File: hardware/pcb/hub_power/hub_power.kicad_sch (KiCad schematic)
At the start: 54 parts, among them J1 XIAO, J10 BAT (JST-PH), J11 → 電源板, J12 → ハブ板, J13 USB-C, J2 OLED, J3 AS5600, J4 SPK IN, J5 SPK OUT, J6 REED, J7 TOGGLE, J8 BTN2, K31 G6S-2F DC5, Q1 MMUN2133LT1G, Q31 SS8050, U1 TPS61090RSAR, U2 MCP73871-2CCI/ML, U3 INA226AIDGSR

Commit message: Extended を 12 → 9 種類に減らす（$36.84 → $27.63）
🔒 2026-09-12 ユーザー「b でいいでしょ」。PowerBoost から写した定数のうち 3 つを Basic の値へ寄せた。
回路の意味はほとんど変えていない。

- R2 340kΩ（C17636・Extended）→ 330kΩ 0603 C23137（Basic）。
  LBO の閾値 0.5×(1+R1/R2) が 3.25V → 3.33V。80mV 早く知らせる側へ動く。
- R6 270kΩ（C17589・Extended）→ 220kΩ 0603 C22961、R7 100kΩ → 82kΩ 0603 C23254（どちらも Basic）。
  VPCC の分圧比 100/370=0.2703 → 82/302=0.2715 で差は 0.45%。
- C6 100µF 10V 1210（C23742・Extended・$0.45）→ 47µF 10V 1206 C96123（Basic・$0.27）を 2 個。
  Basic の 100µF は 6.3V 品しかなく、5.2V が掛かる所で耐圧を下げると残る容量が確実に減る
  （どれだけ減るかは曲線を見ていないので分からない）。耐圧 10V を保つため 2 個に分けた。
  ⚠ 足した C9 は PowerBoost に無い部品で、私が足したもの。

部品は表面実装 44 個・28 種類（Basic 19・Extended 9）。費用は約 $97 → 約 $88。

検査: check_sch 0 件・未配線 0・KiCad DRC のエラー 0（警告 99）・
      check_pcb は下限 0.15mm を割る組 0（いちばん近いのは 0.151mm）。
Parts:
- removed C31: 0.1uF, Capacitor_SMD:C_0805_2012Metric, symbol Device:C_Small
- removed D31: 1N4148W, Diode_SMD:D_SOD-123, symbol Diode:1N4148W
- removed J6: REED, Connector_PinHeader_2.54mm:PinHeader_1x02_P2.54mm_Vertical, symbol Connector_Generic:Conn_01x02
- removed R20: 1K, Resistor_SMD:R_0805_2012Metric, symbol Device:R_Small
- removed R41: 10m, Resistor_SMD:R_1206_3216Metric, symbol Device:R_Small
- removed R44: 5.1k, Resistor_SMD:R_0805_2012Metric, symbol Device:R_Small
- added J1: XIAO, Connector_PinHeader_2.54mm:PinHeader_1x07_P2.54mm_Vertical, symbol Connector_Generic:Conn_01x07
- added J11: → 電源板, Connector_PinHeader_2.54mm:PinHeader_1x07_P2.54mm_Vertical, symbol Connector_Generic:Conn_01x07
- added J13: USB-C, katanori:USB_C_HRO_TYPE-C-31-M-12_NoFrontLegs, symbol Connector:USB_C_Receptacle_USB2.0_16P
- added K31: G6S-2F DC5, Relay_SMD:Relay_DPDT_Omron_G6S-2F, symbol Relay:G6S-2
- added Q1: MMUN2133LT1G, Package_TO_SOT_SMD:SOT-23, symbol Transistor_BJT:Q_PNP_BRT_BEC
- added Q31: SS8050, Package_TO_SOT_SMD:SOT-23, symbol Transistor_BJT:MMBT3904
- added U3: INA226AIDGSR, Package_SO:TSSOP-10_3x3mm_P0.5mm, symbol Sensor_Energy:INA226
- C31: renamed from C32; Note relay_board C2・リードの跳ね止め -> relay_board C1
- C32: renamed from J4; value SPK IN -> 0.1uF; footprint Connector_JST:JST_PH_B2B-PH-K_1x02_P2.00mm_Vertical -> Capacitor_SMD:C_0805_2012Metric; symbol Connector_Generic:Conn_01x02 -> Device:C_Small; LCSC (none) -> C49678; Note IN（ReSpeakerから） -> relay_board C2・リードの跳ね止め
- C41: renamed from R42; value 10K -> 0.1uF; footprint Resistor_SMD:R_0805_2012Metric -> Capacitor_SMD:C_0805_2012Metric; symbol Device:R_Small -> Device:C_Small; LCSC C17414 -> C49678; Note I2C の引き上げ -> (none)
- C6: value 100uF -> 47uF; footprint Capacitor_SMD:C_1210_3225Metric -> Capacitor_SMD:C_1206_3216Metric; LCSC C23742 -> C96123; Note (none) -> PowerBoost C6（100µF 1210）の片割れ
- C7: renamed from R6; value 270K -> 10uF; footprint Resistor_SMD:R_0805_2012Metric -> Capacitor_SMD:C_0805_2012Metric; symbol Device:R_Small -> Device:C_Small; LCSC C17589 -> C15850
- C9: renamed from R3; value 1.87M -> 47uF; footprint Resistor_SMD:R_0805_2012Metric -> Capacitor_SMD:C_1206_3216Metric; symbol Device:R_Small -> Device:C_Small; LCSC C482988 -> C96123; Note (none) -> PowerBoost C6 の片割れ・私が足した（2026-09-12）
- D31: renamed from K31; value G6S-2F DC5 -> 1N4148W; footprint Relay_SMD:Relay_DPDT_Omron_G6S-2F -> Diode_SMD:D_SOD-123; symbol Relay:G6S-2 -> Diode:1N4148W; LCSC C16707 -> C81598; Note COM–NO を使う・NC は空き。2 回路のうち使うのは 1 回路だけ（もう 1 回路は未接続） -> relay_board D1・カソードが +5V（表面実装の 1N4148W）
- J10: renamed from J13; value USB-C -> BAT (JST-PH); footprint katanori:USB_C_HRO_TYPE-C-31-M-12_NoFrontLegs -> Connector_JST:JST_PH_S2B-PH-K_1x02_P2.00mm_Horizontal; symbol Connector:USB_C_Receptacle_USB2.0_16P -> Connector_Generic:Conn_01x02; LCSC C165948 -> (none); Note 充電の口。D+/D− と SBU は使わない -> 🔴 1 番が −・2 番が +（PowerBoost B1 の並び）
- J4: renamed from J5; value SPK OUT -> SPK IN; Note OUT（スピーカーへ） -> IN（ReSpeakerから）
- J5: renamed from J1; value XIAO -> SPK OUT; footprint Connector_PinHeader_2.54mm:PinHeader_1x07_P2.54mm_Vertical -> Connector_JST:JST_PH_B2B-PH-K_1x02_P2.00mm_Vertical; symbol Connector_Generic:Conn_01x07 -> Connector_Generic:Conn_01x02; Note XIAO からの7本 -> OUT（スピーカーへ）
- J6: renamed from J7; value TOGGLE -> REED; Note マスタートグルへ2本 -> リードスイッチへ2本
- J7: renamed from J8; value BTN2 -> TOGGLE; Note 筐体の会話ボタンへ2本 -> マスタートグルへ2本
- J8: renamed from J11; value → 電源板 -> BTN2; footprint Connector_PinHeader_2.54mm:PinHeader_1x07_P2.54mm_Vertical -> Connector_PinHeader_2.54mm:PinHeader_1x02_P2.54mm_Vertical; symbol Connector_Generic:Conn_01x07 -> Connector_Generic:Conn_01x02; Note 板をまたぐ 7 本（2 本目は空き） -> 筐体の会話ボタンへ2本
- LED1: renamed from R5; value 1K -> RED; footprint Resistor_SMD:R_0805_2012Metric -> LED_SMD:LED_0805_2012Metric; symbol Device:R_Small -> Device:LED_Small; LCSC C17513 -> C84256
- LED2: renamed from C8; value 10uF -> WHITE; footprint Capacitor_SMD:C_0805_2012Metric -> LED_SMD:LED_0805_2012Metric; symbol Device:C_Small -> Device:LED_Small; LCSC C15850 -> C34499
- LED3: renamed from R14; value 1K -> GREEN; footprint Resistor_SMD:R_0805_2012Metric -> LED_SMD:LED_0805_2012Metric; symbol Device:R_Small -> Device:LED_Small; LCSC C17513 -> C2297
- LED4: renamed from R8; value 1K -> YELLOW; footprint Resistor_SMD:R_0805_2012Metric -> LED_SMD:LED_0805_2012Metric; symbol Device:R_Small -> Device:LED_Small; LCSC C17513 -> C2296
- R1: renamed from R2; value 340K -> 1.87M; LCSC C17636 -> C482988
- R13: renamed from Q1; value MMUN2133LT1G -> 200K; footprint Package_TO_SOT_SMD:SOT-23 -> Resistor_SMD:R_0805_2012Metric; symbol Transistor_BJT:Q_PNP_BRT_BEC -> Device:R_Small; LCSC C21714196 -> C17539; Note PowerBoost T1（SC-59） -> (none)
- R14: renamed from LED4; value YELLOW -> 1K; footprint LED_SMD:LED_0805_2012Metric -> Resistor_SMD:R_0805_2012Metric; symbol Device:LED_Small -> Device:R_Small; LCSC C2296 -> C17513
- R15: renamed from LED3; value GREEN -> 15K; footprint LED_SMD:LED_0805_2012Metric -> Resistor_SMD:R_0805_2012Metric; symbol Device:LED_Small -> Device:R_Small; LCSC C2297 -> C17475; Note (none) -> PowerBoost THERM
- R16: renamed from R17; value 100K -> 1.0K; LCSC C149504 -> C17513
- R17: renamed from R15; value 15K -> 100K; LCSC C17475 -> C149504; Note PowerBoost THERM -> (none)
- R2: renamed from R13; value 200K -> 330K; LCSC C17539 -> C23137; Note (none) -> PowerBoost は 340kΩ（E96・Extended）。LBO の閾値 0.5×(1+R1/R2) が 3.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
- R20: renamed from LED1; value RED -> 1K; footprint LED_SMD:LED_0805_2012Metric -> Resistor_SMD:R_0805_2012Metric; symbol Device:LED_Small -> Device:R_Small; LCSC C84256 -> C17513
- R3: renamed from R4; value 200K -> 1.87M; LCSC C17539 -> C482988
- R31: renamed from R32; value 10k -> 1k; LCSC C17414 -> C17513; Note relay_board R2・🔴 安全の要 -> relay_board R1
- R32: renamed from Q31; value SS8050 -> 10k; footprint Package_TO_SOT_SMD:SOT-23 -> Resistor_SMD:R_0805_2012Metric; symbol Transistor_BJT:MMBT3904 -> Device:R_Small; LCSC C2150 -> C17414; Note relay_board Q1（2SC1815-GR の表面実装の代わり・SOT-23 は 1=B・2=E・3=C） -> relay_board R2・🔴 安全の要
- R4: renamed from R1; value 1.87M -> 200K; LCSC C482988 -> C17539
- R41: renamed from C41; value 0.1uF -> 10m; footprint Capacitor_SMD:C_0805_2012Metric -> Resistor_SMD:R_1206_3216Metric; symbol Device:C_Small -> Device:R_Small; LCSC C49678 -> C105362; Note (none) -> シャント 10mΩ（今のモジュールと同じ値）
- R43: renamed from J10; value BAT (JST-PH) -> 10K; footprint Connector_JST:JST_PH_S2B-PH-K_1x02_P2.00mm_Horizontal -> Resistor_SMD:R_0805_2012Metric; symbol Connector_Generic:Conn_01x02 -> Device:R_Small; LCSC (none) -> C17414; Note 🔴 1 番が −・2 番が +（PowerBoost B1 の並び） -> I2C の引き上げ
- R44: renamed from R45; Note CC2 の引き下げ -> CC1 の引き下げ（充電器に 5V を出させる）
- R45: renamed from R31; value 1k -> 5.1k; LCSC C17513 -> C27834; Note relay_board R1 -> CC2 の引き下げ
- R5: renamed from LED2; value WHITE -> 1K; footprint LED_SMD:LED_0805_2012Metric -> Resistor_SMD:R_0805_2012Metric; symbol Device:LED_Small -> Device:R_Small; LCSC C34499 -> C17513
- R6: renamed from R7; value 100K -> 220K; LCSC C149504 -> C22961; Note (none) -> PowerBoost は 270kΩ（E96・Extended）。R7 と組で比を保つ
- R7: renamed from R16; value 1.0K -> 82K; LCSC C17513 -> C23254; Note (none) -> PowerBoost は 100kΩ。R6 と組で 100/370=0.2703 → 82/302=0.2715（差 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
- R8: renamed from U3; value INA226AIDGSR -> 1K; footprint Package_SO:TSSOP-10_3x3mm_P0.5mm -> Resistor_SMD:R_0805_2012Metric; symbol Sensor_Energy:INA226 -> Device:R_Small; LCSC C49851 -> C17513; Note A1=VS・A0=GND → 0x44 -> (none)
- renumbered C7 to C8, R43 to R42
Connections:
- net BASE: now also R31.2, Q31.1 (B); no longer R31.1, R45.2
- net BATP: now also J10.2 (Pin_2), R41.1, U3.10 (Vin+); no longer R43.2 (Pin_2), R8.10 (Vin+)
- net BTN: now also J8.2 (Pin_2), J1.1 (Pin_1); no longer J5.1 (Pin_1), J7.2 (Pin_2)
- net CC1: now also R44.1, J13.A5 (CC1); no longer J10.A5 (CC1)
- net CC2: now also R45.1, J13.B5 (CC2); no longer J10.B5 (CC2), R44.1
- net COL: now also D31.2 (A), K31.12, Q31.3 (C); no longer D31.12, R32.3 (C)
- net EN: now also C32.1, J6.2 (Pin_2), J7.1 (Pin_1), J11.7 (Pin_7); no longer C31.1, J6.1 (Pin_1), J8.7 (Pin_7)
- net ENP: now also R13.2; no longer R2.2
- net FB: now also R3.2, R4.1; no longer C9.2, R3.1
- net GND: now also C32.2, J6.1 (Pin_1), J7.2 (Pin_2), J8.1 (Pin_1), J1.5 (Pin_5), J11.3 (Pin_3), Q31.2 (E); no longer J5.5 (Pin_5), J6.2 (Pin_2), J7.1 (Pin_1), J8.3 (Pin_3), R31.2
- net GNDP: now also C41.2, C7.2, C9.2, J10.1 (Pin_1), LED1.1 (K), LED2.1 (K), R15.1, R2.2, R4.2, R45.2, R7.2, J13.A1 (GND), J13.A12 (GND), J13.B1 (GND), J13.B12 (GND), J13.SH (SHIELD), U3.2 (A0), U3.7 (GND); no longer J10.A1 (GND), J10.A12 (GND), J10.B1 (GND), J10.B12 (GND), J10.SH (SHIELD), LED2.2, R1.2, R20.1 (K), R3.2, R41.2, R43.1 (Pin_1), R5.1 (K), R6.2, R7.1, R8.2 (A0), R8.7 (GND)
- net IN: now also R31.1, J1.6 (Pin_6); no longer J5.6 (Pin_6), R45.1
- net LBI: now also R1.2, R2.1; no longer R1.1, R4.2
- net LBO: now also Q1.1 (B); no longer R13.1 (B)
- net N_LED1: now also LED1.2 (A)
- net N_LED2: now also LED2.2 (A); no longer LED1.2
- net N_LED3: now also R14.1; no longer R15.1 (K)
- net N_LED4: now also R8.1; no longer R14.1 (K)
- net N_Q1C: now also R20.1, Q1.3 (C); no longer R13.3 (C)
- net PROG1: now also R16.2; no longer R7.2
- net PROG3: now also R17.2; no longer R16.2
- net SCL: now also J1.3 (Pin_3), J11.6 (Pin_6); no longer J5.3 (Pin_3), J8.6 (Pin_6)
- net SCLP: now also R43.2, U3.5 (SCL); no longer R42.2, R8.5 (SCL)
- net SDA: now also J1.2 (Pin_2), J11.5 (Pin_5); no longer J5.2 (Pin_2), J8.5 (Pin_5)
- net SDAP: now also R42.2, U3.4 (SDA); no longer C41.2, R8.4 (SDA)
- net SPKM: now also J4.2 (Pin_2), J5.1 (Pin_1); no longer C32.2 (Pin_2), J4.1 (Pin_1)
- net SPKO: now also J5.2 (Pin_2), K31.5; no longer D31.5, J4.2 (Pin_2)
- net SPKP: now also J4.1 (Pin_1), K31.4; no longer C32.1 (Pin_1), D31.4
- net STAT1: now also R8.2; no longer LED4.2
- net STAT2: now also R14.2; no longer LED3.2
- net THERM: now also R15.2; no longer R17.2
- net V33: now also J1.4 (Pin_4), J11.4 (Pin_4); no longer J5.4 (Pin_4), J8.4 (Pin_4)
- net V33P: now also R43.1, U3.1 (A1), U3.6 (VS); no longer R41.1, R8.1 (A1), R8.6 (VS)
- net V5: now also C31.1, J1.7 (Pin_7), J11.1 (Pin_1), K31.1; no longer J5.7 (Pin_7), J8.1 (Pin_1)
- net V5P: now also R3.1, R5.1; no longer LED1.1
- net VBUS: now also C8.1, LED3.2 (A), LED4.2 (A), R6.1, J13.A4 (VBUS), J13.A9 (VBUS), J13.B4 (VBUS), J13.B9 (VBUS); no longer C7.1, J10.A4 (VBUS), J10.A9 (VBUS), J10.B4 (VBUS), J10.B9 (VBUS), LED2.1, R14.2 (A), R15.2 (A)
- net VLIPO: now also C7.1, R41.2, U3.8 (Vbus), U3.9 (Vin-); no longer C8.1, R8.8 (Vbus), R8.9 (Vin-)
- net VPCC: now also R6.2, R7.1; no longer C7.2, R6.1
- net VSYS: now also R1.1, R13.1, Q1.2 (E); no longer R13.2 (E), R2.1, R4.1
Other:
- moved on the sheet: C31, C8, J4, J6, J7, R1, R16, R17, R2, R3, R31, R4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

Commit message: J2（OLED）のピンの並びを逆にする — HS154L03W2C01 に合わせて
🔒 2026-09-12 ユーザー。OLED を 1.54" の HS154L03W2C01（SSD1309・I2C・C7465999・$6.94・在庫 1,242）
に替える前提で、J2 だけ並びを逆にした。穴の位置は動かしていない。

  いまの板の J2 : 1 SDA・2 SCL・3 3V3・4 GND
  パネル        : 1 GND・2 VCC・3 SCL・4 SDA（データシート 1.5 Pin Definition）
  逆にした結果  : 1 GND・2 V33・3 SCL・4 SDA

外形はデータシートの図より PCB 42.40 × 38.00 × 2.65、取付穴 φ3.0 × 4（中心間 37.40 × 33.00）、
端子はピッチ 2.54 のスルーホール 4 本。いまの OLED（70.1 × 48.1 × 8.5）より一回り小さく、
高さを決めていた 48.1 が 38 になる。

⚠ いまの OLED の線はこの板に挿せなくなる。戻すなら gen_sch.py の PORT_FLIP を空にする。
⚠ check_sch.py は PORT_FLIP を読んで同じ並びを期待するので、この 1 か所は機械で検算していない。

検査: check_sch 0 件・未配線 0・DRC エラー 0（警告 99）・check_pcb 0.151mm。
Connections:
- net GND: now also J2.1 (Pin_1); no longer J2.4 (Pin_4)
- net SCL: now also J2.3 (Pin_3); no longer J2.2 (Pin_2)
- net SDA: now also J2.4 (Pin_4); no longer J2.1 (Pin_1)
- net V33: now also J2.2 (Pin_2); no longer J2.3 (Pin_3)
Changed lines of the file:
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@@
 		)
 	)
-	(label "SDA"
+	(label "GND"
 		(at 127.00 241.30 180)
 		(effects
@@
 		)
 	)
-	(label "SCL"
+	(label "V33"
 		(at 127.00 243.84 180)
 		(effects
@@
 		)
 	)
-	(label "V33"
+	(label "SCL"
 		(at 127.00 246.38 180)
 		(effects
@@
 		)
 	)
-	(label "GND"
+	(label "SDA"
 		(at 127.00 248.92 180)
 		(effects

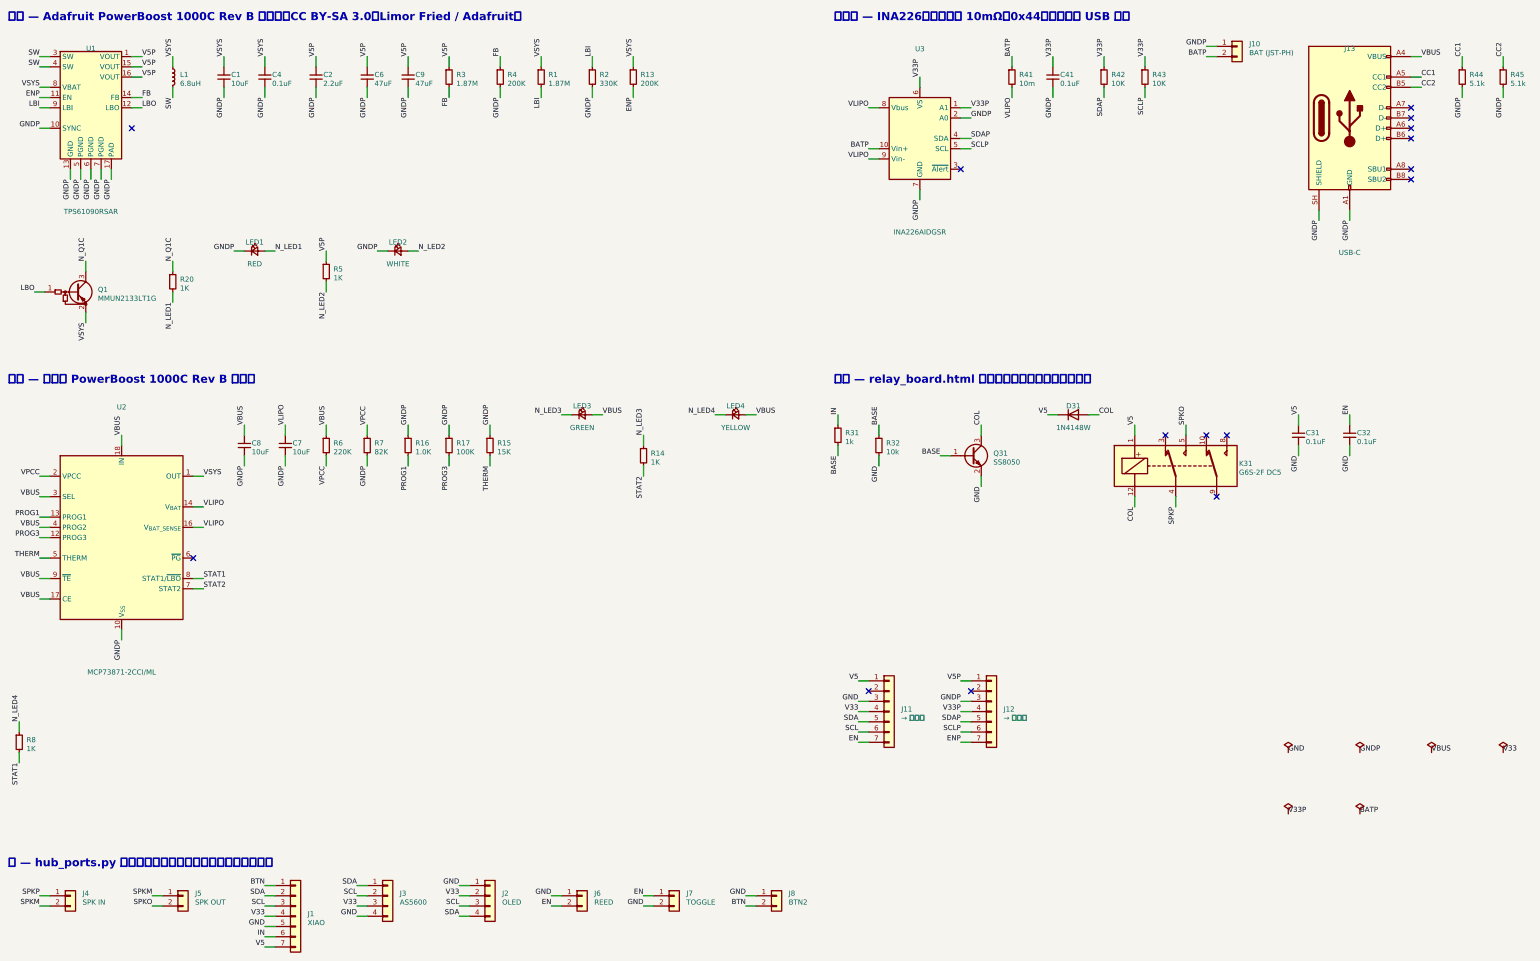
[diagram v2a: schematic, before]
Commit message: 回路図を v6 の 1 枚板に直す（電源統合・AS5600 チップ・スライドスイッチ・XIAO 直挿し）
🔒 ユーザー 2026-09-13「歯車 3 枚」。幅 48・板 44 × 81.2 で確定したので回路図を起こし直した。

- 板は 1 枚。J11 / J12（板をまたぐ 7 本 × 2）を削除し、板ごとの別名ネット
  （V5P・GNDP・V33P・SDAP・SCLP・ENP）を廃止。USB-C まわりに直書きされていた
  GNDP も GND に戻した
- J3（AS5600 の口）→ U4 AS5600-ASOM のチップ ＋ C42 100nF。
  📄 データシート 9 ページ Figure 13「In 3.3V operation, the VDD5V and VDD3V3 pins
  must be tied together」に従って 1 番と 2 番を V33 へ。DIR=GND・OUT と PGO は未接続
- J7（トグルの口）→ SW1 スライドスイッチ（MST-12D18G3・C49023766）。COM を EN・
  片側を GND へ。リードスイッチと並列
- J2（OLED）を JST PH の 4 ピン横型へ。🔴 ピンの並び 1 GND・2 VCC・3 SCL・4 SDA は維持
- スピーカー IN / OUT の PH を縦挿しから横挿しへ（背 6.0 → 4.8）
- XIAO の口を直挿しの 2 列 14 本（J1 = D0〜D6 側・J14 = 5V/GND/3V3/D10〜D7 側）へ。
  🔴 どちらの列かは鏡像事故の温床なので、出どころ 3 つ（筐体側の 3 次元変換・XIAO の
  標準上面図の 90° 回転・RESPEAKER-LITE.md 3 章の外部パッドの位置）が一致するのを
  確かめてから書いた
- check_sch.py: 板をまたぐ口の検査を捨て、XIAO の 2 列 14 本（gen_sch の表を読んで
  突き合わせる）と AS5600 / トグルの検査を足した
- kisym.py がスクリプトの隣の katanori.kicad_sym も読むようにして、KiCad の標準に
  無い AS5600 の記号をそこに作った

check_sch は 0 件。ERC は pin_not_driven 1（Q1・元からある）と、
CLI にライブラリ表が無いことによる警告だけ。

⬜ 次: スライドスイッチの足形（katanori:SW_Slide_MST-12D18G3）はまだ作っていない。
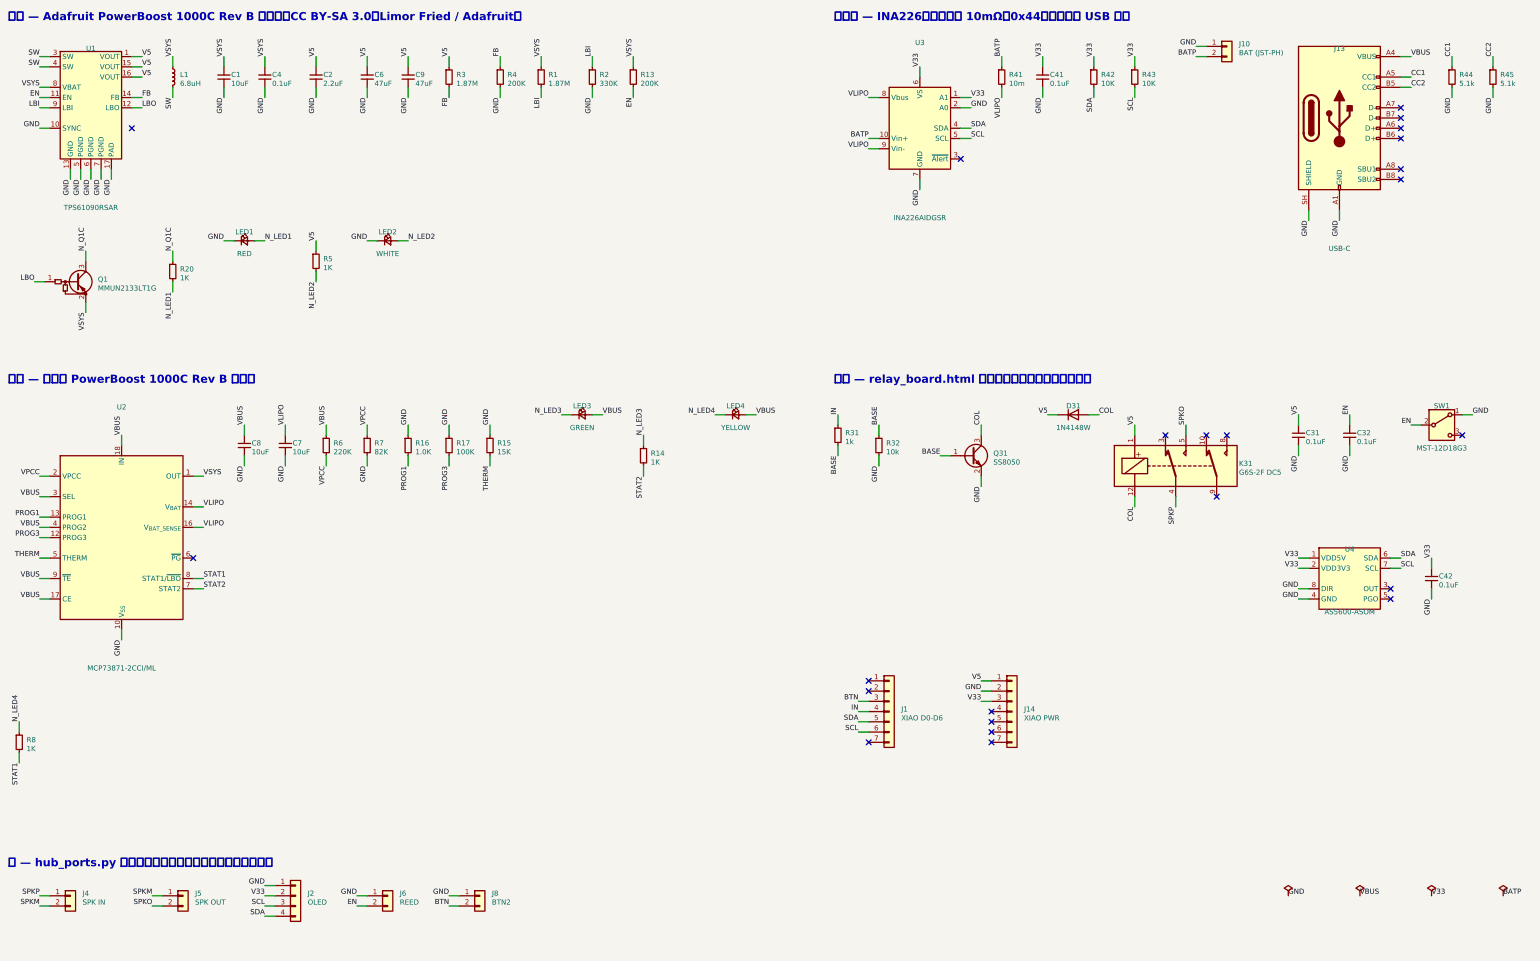
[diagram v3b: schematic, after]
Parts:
- removed J11: → 電源板, Connector_PinHeader_2.54mm:PinHeader_1x07_P2.54mm_Vertical, symbol Connector_Generic:Conn_01x07
- removed J12: → ハブ板, Connector_PinHeader_2.54mm:PinHeader_1x07_P2.54mm_Vertical, symbol Connector_Generic:Conn_01x07
- removed J3: AS5600, Connector_PinHeader_2.54mm:PinHeader_1x04_P2.54mm_Vertical, symbol Connector_Generic:Conn_01x04
- removed J7: TOGGLE, Connector_PinHeader_2.54mm:PinHeader_1x02_P2.54mm_Vertical, symbol Connector_Generic:Conn_01x02
- added C42: 0.1uF, Capacitor_SMD:C_0805_2012Metric, symbol Device:C_Small
- added J14: XIAO PWR, Connector_PinSocket_2.54mm:PinSocket_1x07_P2.54mm_Vertical, symbol Connector_Generic:Conn_01x07
- added J4: SPK IN, Connector_JST:JST_PH_S2B-PH-K_1x02_P2.00mm_Horizontal, symbol Connector_Generic:Conn_01x02
- added SW1: MST-12D18G3, katanori:SW_Slide_MST-12D18G3, symbol Switch:SW_SPDT
- J1: value XIAO -> XIAO D0-D6; footprint Connector_PinHeader_2.54mm:PinHeader_1x07_P2.54mm_Vertical -> Connector_PinSocket_2.54mm:PinSocket_1x07_P2.54mm_Vertical; Note XIAO からの7本 -> 列 X 9.4・1 本目が Y 2.90 側: D0 / D1 / D2 / D3 / D4 / D5 / D6
- J2: footprint Connector_PinHeader_2.54mm:PinHeader_1x04_P2.54mm_Vertical -> Connector_JST:JST_PH_S4B-PH-K_1x04_P2.00mm_Horizontal
- J5: footprint Connector_JST:JST_PH_B2B-PH-K_1x02_P2.00mm_Vertical -> Connector_JST:JST_PH_S2B-PH-K_1x02_P2.00mm_Horizontal
- J6, J8: footprint Connector_PinHeader_2.54mm:PinHeader_1x02_P2.54mm_Vertical -> Connector_PinSocket_2.54mm:PinSocket_1x02_P2.54mm_Horizontal
- U4: renamed from J4; value SPK IN -> AS5600-ASOM; footprint Connector_JST:JST_PH_B2B-PH-K_1x02_P2.00mm_Vertical -> Package_SO:SOIC-8_3.9x4.9mm_P1.27mm; symbol Connector_Generic:Conn_01x02 -> katanori:AS5600-ASOM; LCSC (none) -> C79815; Note IN（ReSpeakerから） -> つまみの角度。磁石は真上・板 X 36.2 Y 7。🔴 PGO(5) と OUT(3) は繋がない
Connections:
- net ENP is gone; now on net EN: R13.2, U1.11 (EN)
- net GNDP is gone; now on net GND: C1.2, C2.2, C4.2, C41.2, C6.2, C7.2, C8.2, C9.2, J10.1 (Pin_1), J13.A1 (GND), J13.A12 (GND), J13.B1 (GND), J13.B12 (GND), J13.SH (SHIELD), LED1.1 (K), LED2.1 (K), R15.1, R16.1, R17.1, R2.2, R4.2, R44.2, R45.2, R7.2, U1.10 (SYNC), U1.13 (GND), U1.17 (PAD), U1.5 (PGND), U1.6 (PGND), U1.7 (PGND), U2.10 (V_{SS}), U2.11 (V_{SS}), U2.21 (V_{SS}), U3.2 (A0), U3.7 (GND)
- net SCLP is gone; now on net SCL: R43.2, U3.5 (SCL)
- net SDAP is gone; now on net SDA: R42.2, U3.4 (SDA)
- net V33P is gone; now on net V33: C41.1, R42.1, R43.1, U3.1 (A1), U3.6 (VS)
- net V5P is gone; now on net V5: C2.1, C6.1, C9.1, R3.1, R5.1, U1.1 (VOUT), U1.15 (VOUT), U1.16 (VOUT)
- net BTN: now also J1.3 (Pin_3); no longer J1.1 (Pin_1)
- net EN: now also SW1.2 (B)
- net GND: now also U4.4 (GND), U4.8 (DIR), C42.2, J14.2 (Pin_2), SW1.1 (A); no longer J1.5 (Pin_5)
- net IN: now also J1.4 (Pin_4); no longer J1.6 (Pin_6)
- net SCL: now also J1.6 (Pin_6), U4.7 (SCL); no longer J1.3 (Pin_3)
- net SDA: now also J1.5 (Pin_5), U4.6 (SDA); no longer J1.2 (Pin_2)
- net SPKM: now also J4.2 (Pin_2); no longer U4.2 (Pin_2)
- net SPKP: now also J4.1 (Pin_1); no longer U4.1 (Pin_1)
- net V33: now also U4.1 (VDD5V), U4.2 (VDD3V3), C42.1, J14.3 (Pin_3); no longer J1.4 (Pin_4)
- net V5: now also J14.1 (Pin_1); no longer J1.7 (Pin_7)
- no-connect marks 15 -> 23
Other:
- moved on the sheet: C41, J10, J13, LED1, LED2, Q1, R20, R41, R42, R43, R44, R45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

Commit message: リードと会話ボタンを 1 つの 4 ピン PH にまとめて、口 5 つを全部挿せるようにする
🔒 ユーザー 2026-09-13「別に線が二股になるのは構わないと思います」。

- 3 ピン（EN・BTN・GND）ではなく 4 ピンにした。GND を 2 本にすれば、1 つの端子へ線を
  2 本入れることも、線を割って継ぐこともせずに済む。並びは隣り合う 2 本ずつで分かれる
  ように 1 EN・2 GND →リード ／ 3 GND・4 BTN →会話ボタン
- 4 ピンの PH は幅 10.90 で、入るのは谷（幅 11.6）と上の縁（幅 12）の 2 か所だけ。
  OLED を上の縁、リード＋会話ボタンを谷にした
- スピーカーは箱の左なので、スピーカーへ出る J5 を左の帯に。ReSpeaker から来る J4 は右の帯へ

🔴 途中で J6 が 2 つできていた。PORT_REF から REED/BTN2 を外す編集が assert で止まって
書かれておらず、hub_ports 由来の J6（2 ピン）と新しい J6（4 ピン）が同じ ref で並び、
EN が GND に飲まれていた。check_sch が捕まえた。

結果: プラグの通り道 5 口すべて空き（J2 だけ通り道が電池の下で、挿し直すには電池を外す）。
配線 649 本・未配線 0・DRC エラー 0・check_sch 0 件・
check_pcb は下限 0.15mm に対していちばん近いのが 0.152mm。
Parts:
- removed J8: BTN2, Connector_PinSocket_2.54mm:PinSocket_1x02_P2.54mm_Horizontal, symbol Connector_Generic:Conn_01x02
- J6: value REED -> REED+BTN2; footprint Connector_PinSocket_2.54mm:PinSocket_1x02_P2.54mm_Horizontal -> Connector_JST:JST_PH_S4B-PH-K_1x04_P2.00mm_Horizontal; symbol Connector_Generic:Conn_01x02 -> Connector_Generic:Conn_01x04; Note リードスイッチへ2本 -> 1 EN・2 GND → リード ／ 3 GND・4 BTN → 会話ボタン（線は口の所で二股）
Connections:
- net BTN: now also J6.4 (Pin_4)
- net EN: now also J6.1 (Pin_1); no longer J6.2 (Pin_2)
- net GND: now also J6.2 (Pin_2), J6.3 (Pin_3); no longer J6.1 (Pin_1)
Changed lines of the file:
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@@
 	)
 	(symbol
-		(lib_id "Connector_Generic:Conn_01x02")
+		(lib_id "Connector_Generic:Conn_01x04")
 		(at 109.22 243.84 0)
 		(unit 1)
@@
 			)
 		)
-		(property "Value" "REED"
+		(property "Value" "REED+BTN2"
 			(at 112.22 245.44 0)
 			(effects
@@
 			)
 		)
-		(property "Footprint" "Connector_PinSocket_2.54mm:PinSocket_1x02_P2.54mm_Horizontal"
+		(property "Footprint" "Connector_JST:JST_PH_S4B-PH-K_1x04_P2.00mm_Horizontal"
 			(at 109.22 243.84 0)
 			(effects
@@
 			)
 		)
-		(property "Note" "リードスイッチへ2本"
+		(property "Note" "1 EN・2 GND → リード ／ 3 GND・4 BTN → 会話ボタン（線は口の所で二股）"
 			(at 109.22 243.84 0)
 			(effects
@@
 		(pin "2"
 		)
+		(pin "3"
+		)
+		(pin "4"
+		)
 		(instances
 			(project "hub_power"
@@
 				)
 			)
+		)
+	)
+	(wire
+		(pts
+			(xy 104.14 241.30)
+			(xy 101.60 241.30)
+		)
+		(stroke
+			(width 0)
+			(type default)
+		)
+	)
+	(label "EN"
+		(at 101.60 241.30 180)
+		(effects
+			(font
+				(size 1.27 1.27)
+			)
+			(justify right bottom)
 		)
 	)
@@
 		)
 	)
-	(label "EN"
+	(label "GND"
 		(at 101.60 246.38 180)
-		(effects
-			(font
-				(size 1.27 1.27)
-			)
-			(justify right bottom)
-		)
-	)
-	(symbol
-		(lib_id "Connector_Generic:Conn_01x02")
-		(at 132.08 243.84 0)
-		(unit 1)
-		(exclude_from_sim no)
-		(in_bom yes)
-		(on_board yes)
-		(dnp no)
-		(property "Reference" "J8"
-			(at 135.08 243.24 0)
-			(effects
-				(font
-					(size 1.27 1.27)
-				)
-				(justify left)
-			)
-		)
-		(property "Value" "BTN2"
-			(at 135.08 245.44 0)
-			(effects
-				(font
-					(size 1.27 1.27)
-				)
-				(justify left)
-			)
-		)
-		(property "Footprint" "Connector_PinSocket_2.54mm:PinSocket_1x02_P2.54mm_Horizontal"
-			(at 132.08 243.84 0)
-			(effects
-				(font
-					(size 1.27 1.27)
-				)
-				(hide yes)
-			)
-		)
-		(property "Datasheet" ""
-			(at 132.08 243.84 0)
-			(effects
-				(font
-					(size 1.27 1.27)
-				)
-				(hide yes)
-			)
-		)
-		(property "Note" "筐体の会話ボタンへ2本"
-			(at 132.08 243.84 0)
-			(effects
-				(font
-					(size 1.27 1.27)
-				)
-				(hide yes)
-			)
-		)
-		(pin "1"
-		)
-		(pin "2"
-		)
-		(instances
-			(project "hub_power"
-				(path "/66b6a92b-a6ed-51a0-a5cc-19571fa30d54"
-					(reference "J8")
-					(unit 1)
-				)
-			)
-		)
-	)
-	(wire
-		(pts
-			(xy 127.00 243.84)
-			(xy 124.46 243.84)
-		)
-		(stroke
-			(width 0)
-			(type default)
-		)
-	)
-	(label "GND"
-		(at 124.46 243.84 180)
 		(effects
 			(font
@@
 	(wire
 		(pts
-			(xy 127.00 246.38)
-			(xy 124.46 246.38)
+			(xy 104.14 248.92)
+			(xy 101.60 248.92)
 		)
 		(stroke
@@
 	)
 	(label "BTN"
-		(at 124.46 246.38 180)
+		(at 101.60 248.92 180)
 		(effects
 			(font

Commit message: C42 の LCSC 番号が抜けていた（fab.py が止まって気づいた）
AS5600 のパスコン C42 に番号が無く、部品表を作ろうとすると
「LCSC の番号が無い表面実装の部品: C42」で止まっていた。C49678（0.1µF 50V・Basic）を入れた。

⇒ 部品表 30 種類・47 個。実装を頼まないのは J1・J2・J4・J5・J6・J10・J14 の 7 つ
（全部スルーホールの口で、自分で付ける）。
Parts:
- C42: LCSC (none) -> C49678
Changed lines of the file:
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@@
+			)
+		)
+		(property "LCSC" "C49678"
+			(at 368.30 165.10 0)
+			(effects
+				(font
+					(size 1.27 1.27)
+				)
+				(hide yes)
 			)
 		)
